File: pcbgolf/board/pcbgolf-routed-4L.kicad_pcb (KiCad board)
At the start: 2 copper layers, 48.2 x 51 mm, 245 parts, among them J1 DCBARRELSMT, J2 MICRO_SD-0472192001, J3 USB-C-FEMALE, J4 CAN, J5 USB-C-FEMALEGCT, J6 USB-C-FEMALEGCT, J7 USB-C-FEMALEGCT, J8 USB-C-FEMALEGCT, Q1 SIS427-VI, Q2 NFET-DUAL-COMMON-SOURCE-QS5K2, Q3 NFET-DUAL-COMMON-SOURCE-QS5K2, Q4 NFET-DUAL-COMMON-SOURCE-QS5K2, Q5 NFET-DUAL-COMMON-SOURCE-QS5K2, Q6 NFET-DUAL-COMMON-SOURCE-QS5K2, Q7 NFET-DUAL-COMMON-SOURCE-QS5K2, Q8 NFET-DUAL-COMMON-SOURCE-QS5K2, Q9 NFET-DUAL-COMMON-SOURCE-QS5K2, SW1 SPST-2-4PIN, U1 AP62300T, U10 NCS20071XV, U11 NCS20071XV, U12 NCS20071XV, U13 TPS25942, U14 TPS25942, U15 TPS25942, U16 TPS25942, U2 AP62300T, U3 STM32H725ZGTx, U4 USB2517, U5 MCP2542FDT-E/MNY, U6 MCP2542FDT-E/MNY, U7 MCP2542FDT-E/MNY, U8 MCP2542FDT-E/MNY, U9 NCS20071XV, Y1 25MHz, Y2 24MHz

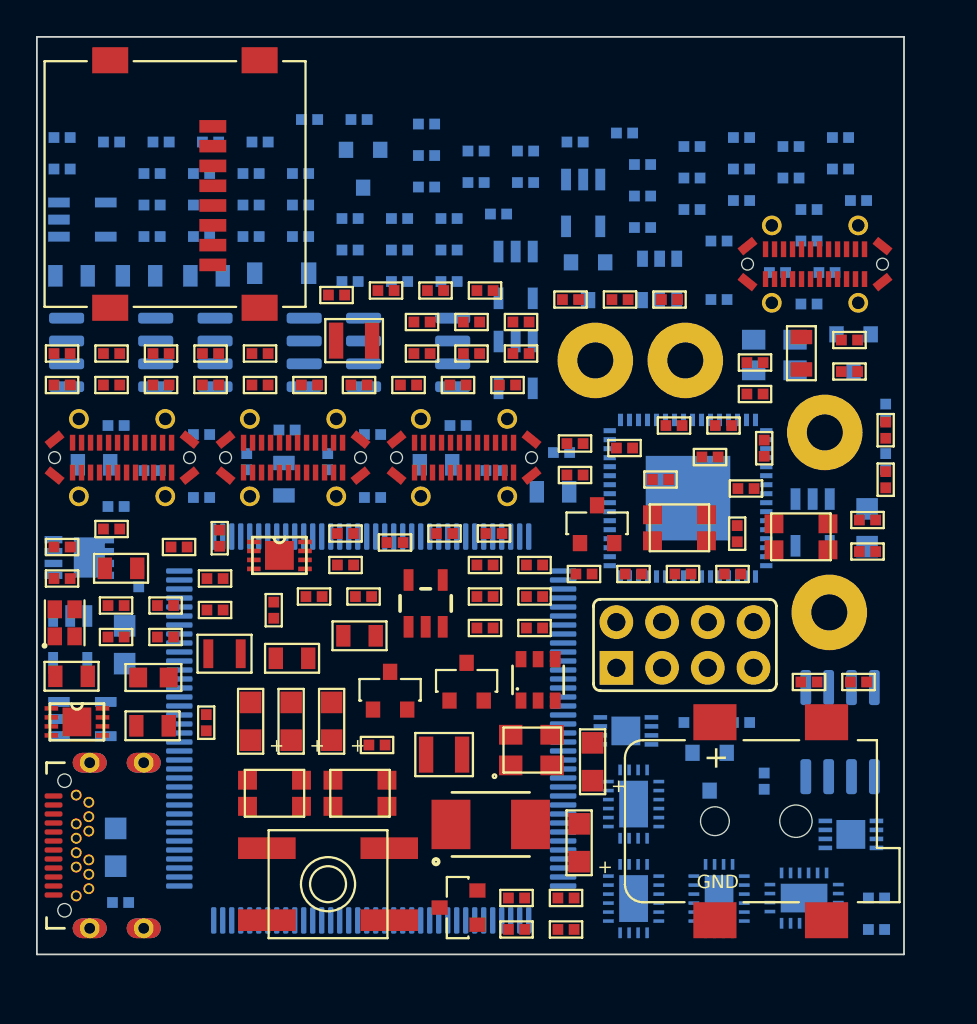
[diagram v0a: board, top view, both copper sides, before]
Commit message: Sync pcbgolf: measured part heights, 3D assembly bounding box, final board
Mirrors lblommesteyn/pcbgolf. The substantive change is that part heights are
now measured from the footprints' own STEP models rather than estimated: the
barrel jack is 11.00 mm, not the 9.00 mm assumed, so Z is 14.35 mm and every
previously reported volume was understated by about 5,300 mm^3.

Also adds bbox3d.py (the real PCBA bounding box, which is what the challenge
scores), step_assembly.py (a STEP built from that same geometry), and the
final LQFP-100 board with R11 not fitted, since the LQFP-100 package has no
PDR_ON pin for it to strap.

Co-Authored-By: Claude Opus 5 <noreply@anthropic.com>
Claude-Session: https://claude.ai/code/session_013nBHDXVrXKghy52w5PgN3h
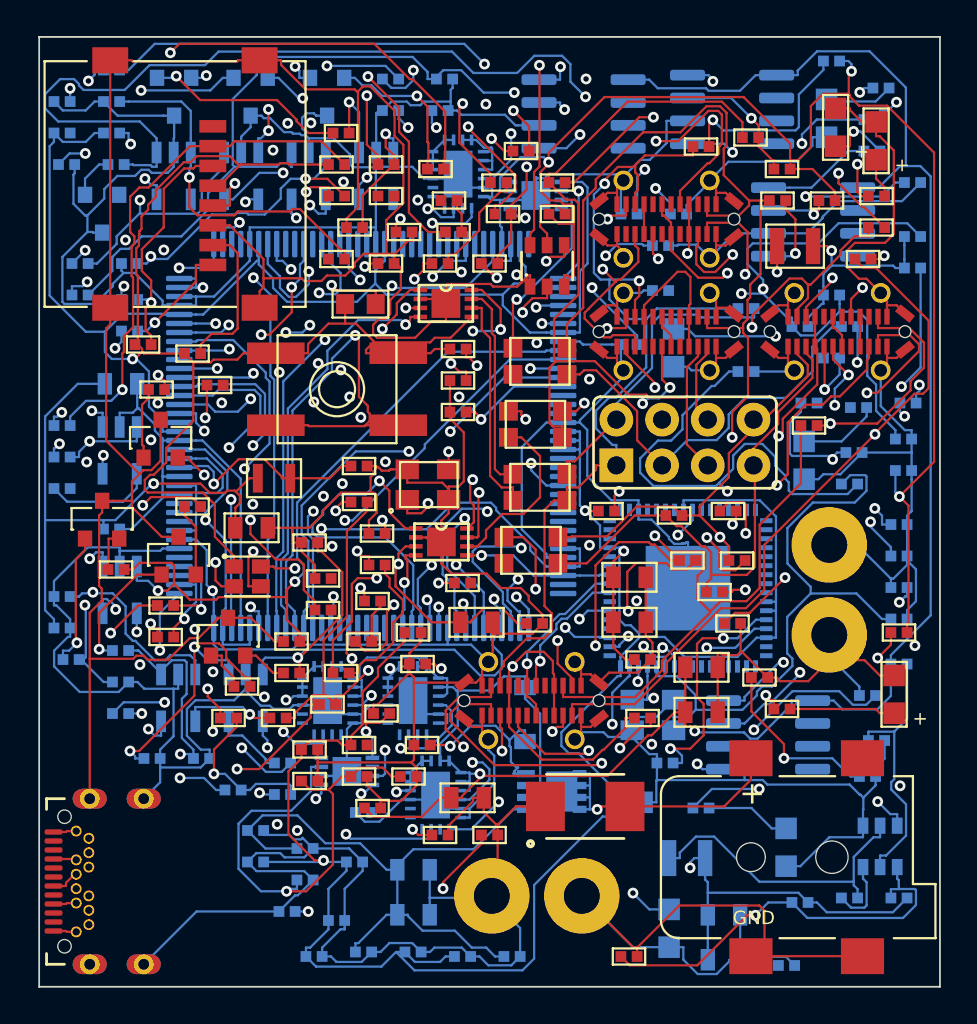
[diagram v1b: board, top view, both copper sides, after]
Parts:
- C11, C24, C31, L2, LED2, LED7, Q6, R119, R87: moved to B.Cu
- C13, C39, R2, R65, R66: moved to F.Cu
- moved C16 51.1 mm to (51.2, 82.5)
- moved C9 50.9 mm to (95.0, 97.5)
- moved C45 50.7 mm to (65.2, 100.8)
- moved R31 48.6 mm to (97.7, 76.8)
- moved C27 48.5 mm to (70.7, 100.5)
- moved C12 48.1 mm to (88.0, 98.5)
- moved LED3 46.3 mm to (94.2, 54.7)
- moved R8 45.7 mm to (96.5, 88.8)
- moved LED15 45.3 mm to (61.7, 53.0)
- moved C48 45.2 mm to (64.7, 94.8)
- moved C1 44.5 mm to (88.0, 101.0)
- moved C35 43.3 mm to (63.7, 98.3), turned to 0 degrees
- moved U14 42.8 mm to (73.2, 57.3)
- moved R119 42.8 mm to (94.0, 67.5)
- moved LED2 42.5 mm to (93.7, 54.2)
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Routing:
- net GND: track 0.00 -> 863.8 mm
- net +3V3: track 0.00 -> 385.6 mm, vias 0 -> 10
- net +5V: track 0.00 -> 271.4 mm, vias 0 -> 7
- net +12V: track 0.00 -> 183.3 mm, vias 0 -> 3
- net CAN3_L: track 0.00 -> 114.1 mm, vias 0 -> 3
- net CAN2_H: track 0.00 -> 110.6 mm, vias 0 -> 5
- net VDDLDO: track 0.00 -> 105.4 mm, vias 0 -> 4
- net CAN2_L: track 0.00 -> 100.1 mm, vias 0 -> 3
- net CH1_SBU1: track 0.00 -> 93.5 mm, vias 0 -> 4
- net CH3_SBU1: track 0.00 -> 91.6 mm, vias 0 -> 2
- net CAN1_H: track 0.00 -> 89.5 mm, vias 0 -> 3
- net CH2_SBU1_IGN: track 0.00 -> 88.0 mm, vias 0 -> 3
- net CH4_SBU2: track 0.00 -> 86.7 mm, vias 0 -> 3
- net CAN0_H: track 0.00 -> 83.3 mm, vias 0 -> 4
- net N$237: track 0.00 -> 77.8 mm, vias 0 -> 3
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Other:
- board size 48.2 x 51 mm -> 50 x 52.8 mm
- copper layers 2 -> 4
